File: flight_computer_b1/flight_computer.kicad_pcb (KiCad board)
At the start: 4 copper layers, 78 x 67 mm, 102 parts, among them J1 DB25_Socket, J2 DB25_Socket, J3 Conn_01x03, J4 Screw_Terminal_01x02, J5 Pi Connector, J6 Conn_02x02_Odd_Even, Q3 ISA170230C04LMDS, U1 IRLML6344TRPBF, U10 LTC2983, U11 CD74HC4067SM, U12 IRLML6344TRPBF, U2 IRLML6344TRPBF, U3 IRLML6344TRPBF, U4 IRLML6344TRPBF, U5 LMR51430XFDDCR, U6 MCP6001-OT, U7 MCP6001-OT, U8 ADS1158IRTCR, U9 LM66200DRLR, Y1 32.768kHz

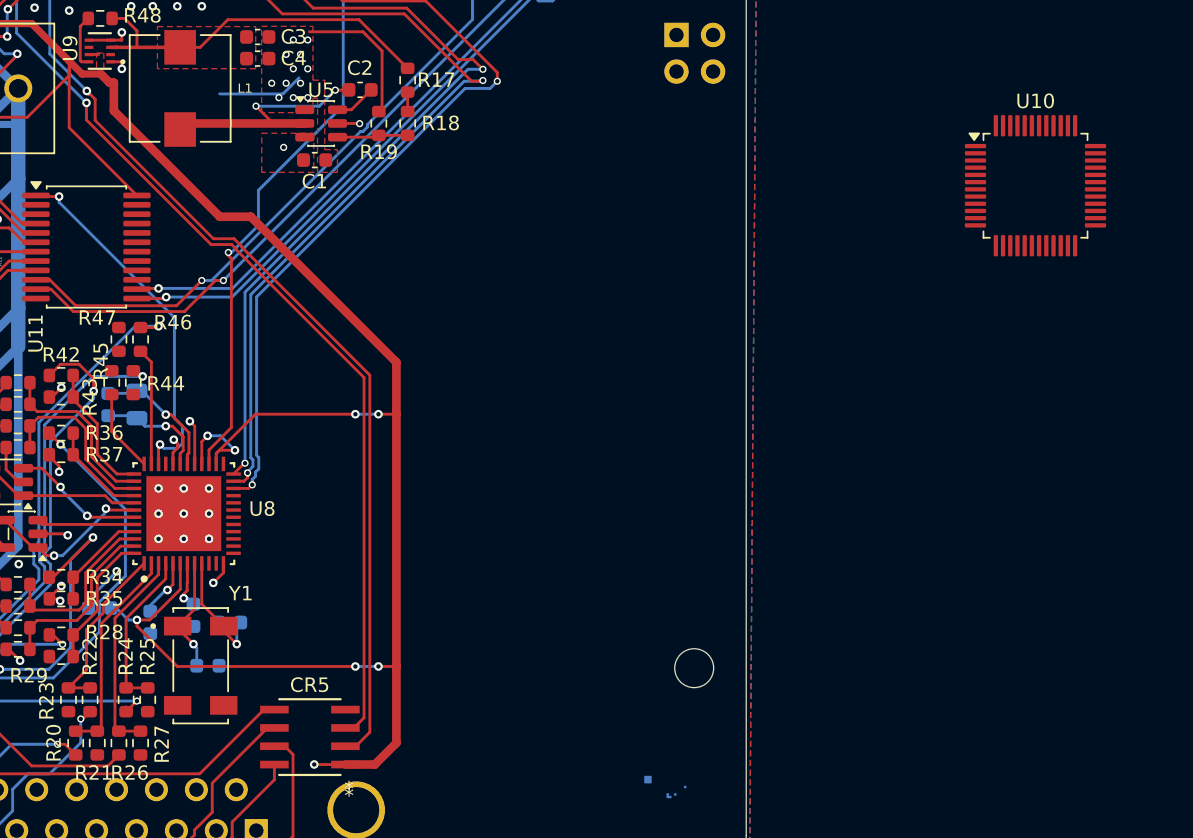
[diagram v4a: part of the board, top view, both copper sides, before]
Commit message: assigned footprints to capacitors
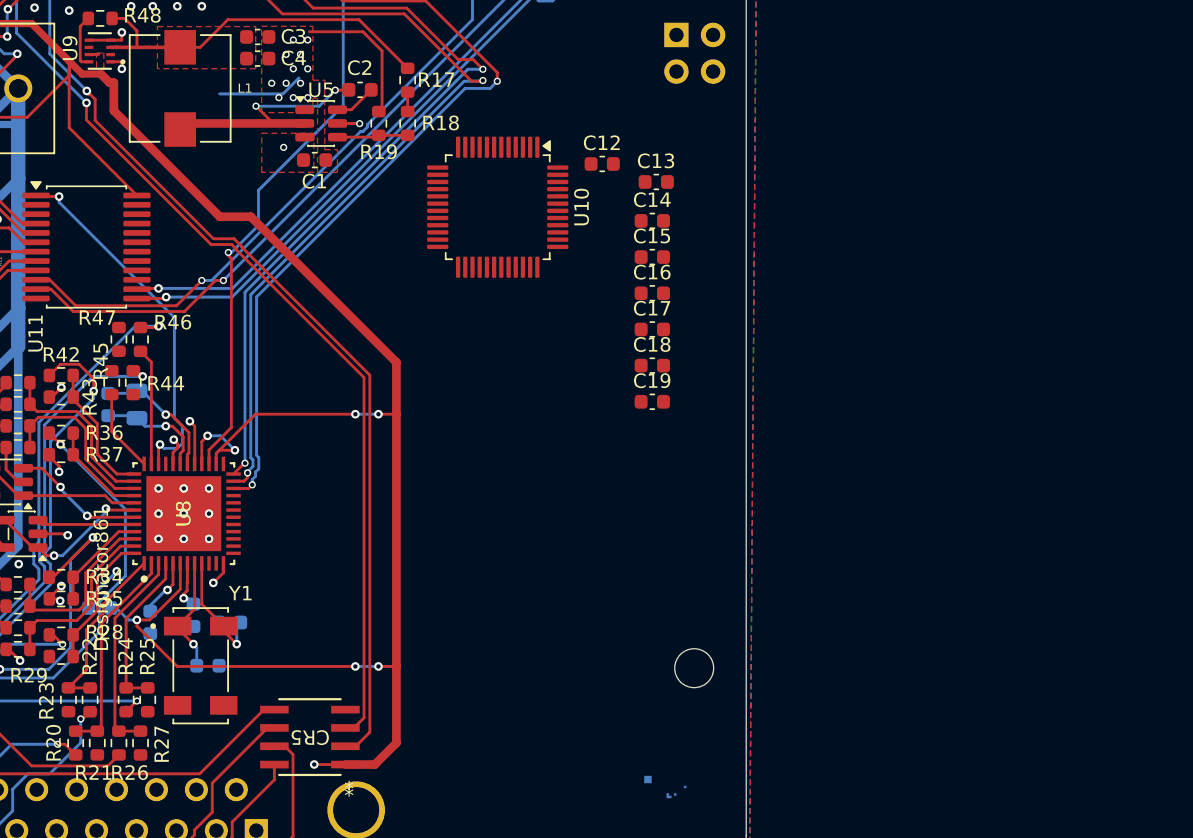
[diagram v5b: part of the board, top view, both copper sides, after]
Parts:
- added C12: 10uF, Capacitor_SMD:C_0603_1608Metric, F.Cu at (170.5, 88.8)
- added C13: 10uF, Capacitor_SMD:C_0603_1608Metric, F.Cu at (174.2, 90.0)
- added C14: 10uF, Capacitor_SMD:C_0603_1608Metric, F.Cu at (174.0, 92.7)
- added C15: 10uF, Capacitor_SMD:C_0603_1608Metric, F.Cu at (174.0, 95.2)
- added C16: 0.1uF, Capacitor_SMD:C_0603_1608Metric, F.Cu at (174.0, 97.7)
- added C17: 0.1uF, Capacitor_SMD:C_0603_1608Metric, F.Cu at (174.0, 100.2)
- added C18: 0.1uF, Capacitor_SMD:C_0603_1608Metric, F.Cu at (174.0, 102.7)
- added C19: 0.1uF, Capacitor_SMD:C_0603_1608Metric, F.Cu at (174.0, 105.2)
- CR5: footprint avi_lib:SO-8_STM -> avi_footprint:SO-8_STM
- U8: footprint avi_lib:RTC0048A-IPC_A -> avi_footprint:RTC0048A-IPC_A
- moved U10 37.3 mm to (163.2, 91.8), turned to -90 degrees

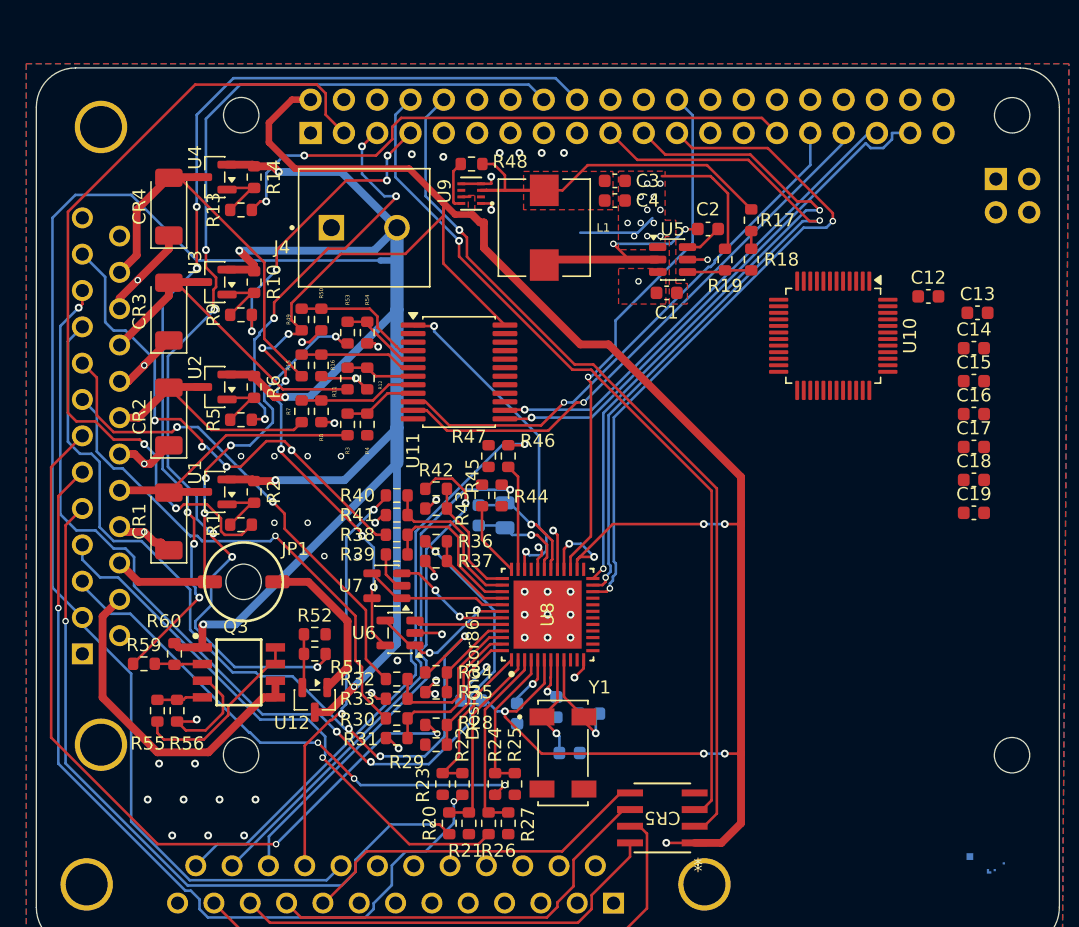
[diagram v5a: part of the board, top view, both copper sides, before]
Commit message: routed traces for pi & fixed many DRC issues
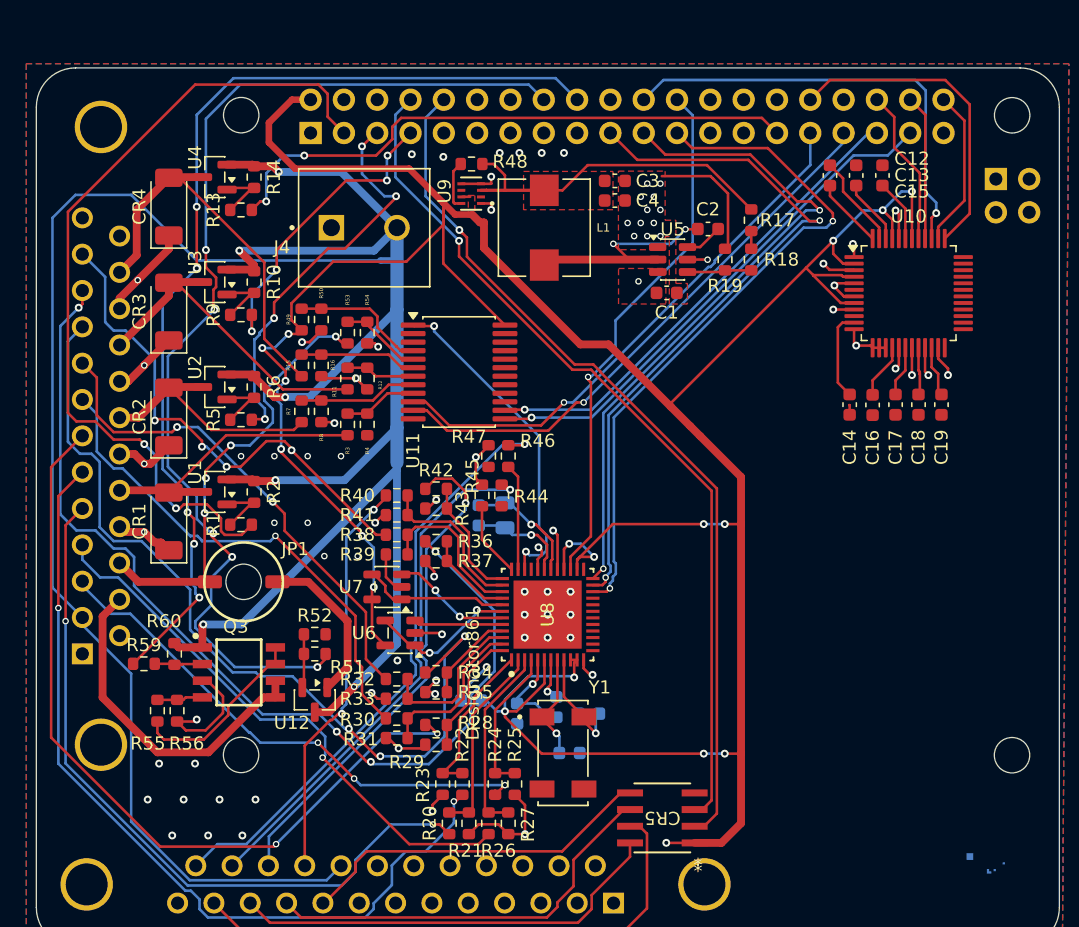
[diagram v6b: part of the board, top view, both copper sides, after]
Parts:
- moved C15 17.2 mm to (167.0, 79.5), turned to 90 degrees
- moved C13 14.0 mm to (165.0, 79.5), turned to 90 degrees
- moved C12 11.9 mm to (163.0, 79.5), turned to 90 degrees
- moved C14 10.4 mm to (164.5, 97.0), turned to -90 degrees
- moved C19 8.61 mm to (171.5, 97.0), turned to -90 degrees
- moved C16 7.76 mm to (166.2, 97.0), turned to -90 degrees
- moved C18 7.13 mm to (169.8, 97.0), turned to -90 degrees
- moved C17 6.79 mm to (168.0, 97.0), turned to -90 degrees
- moved U10 6.60 mm to (169.0, 88.5), turned to 0 degrees
- moved U7 0.09 mm to (129.2, 110.9)
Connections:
- J5 pad 22: unconnected-(J5-Pin_22-Pad22) -> /TEMP_DOUT
- J5 pad 32: unconnected-(J5-Pin_32-Pad32) -> /TEMP_INT
- J5 pad 35: /TEMP_DOUT -> /mux_addr2
- J5 pad 37: unconnected-(J5-Pin_37-Pad37) -> /mux_addr3
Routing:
- net +5V: track 193.3 -> 244.8 mm, vias 14 -> 18
- net GND: track 182.2 -> 219.4 mm, vias 70 -> 83
- net /TEMP_DOUT: track 0.00 -> 34.2 mm, vias 0 -> 1
- net /TEMP_INT: track 0.00 -> 24.6 mm
- net /TEMP_SCLK: track 0.00 -> 12.1 mm
- net /TEMP_CS: track 0.00 -> 12.0 mm
- net /TEMP_DIN: track 0.00 -> 11.1 mm
- net Net-(U10-Q2): track 0.00 -> 7.14 mm
- net Net-(U10-V_{REF_BYP}): track 0.00 -> 6.88 mm
- net Net-(U10-Q1): track 0.00 -> 5.38 mm
- net Net-(U10-Q3): track 0.00 -> 4.97 mm
- net Net-(U10-LDO): track 0.00 -> 4.76 mm
- net /TC1+: track 0.00 -> 4.21 mm
- net /TC4+: track 0.00 -> 3.87 mm
- net /TC2+: track 0.00 -> 3.87 mm
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
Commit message: net updates
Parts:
- removed G***: LOGO, avi_lib:qr-code
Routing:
- net GND: vias 83 -> 85

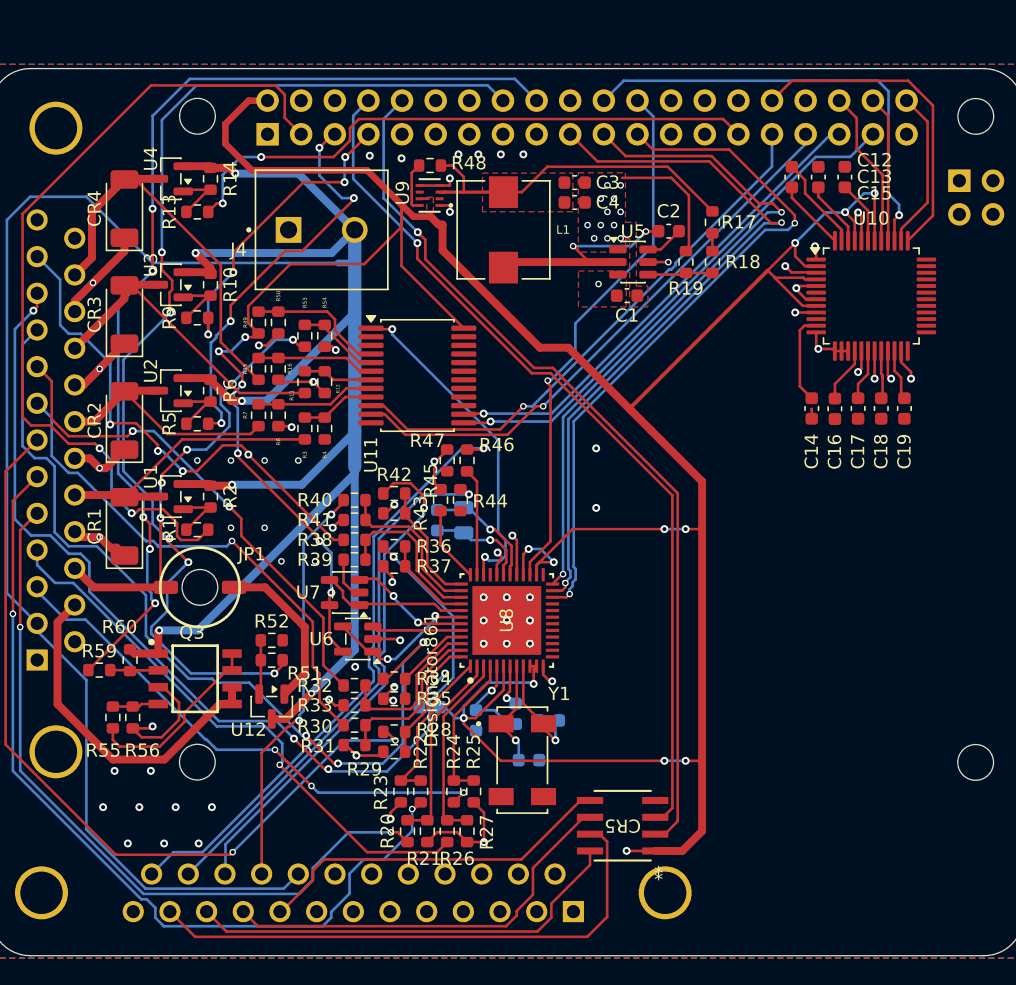
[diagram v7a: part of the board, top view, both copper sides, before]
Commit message: routed pi traces, fixed all unavoidable DRC errors
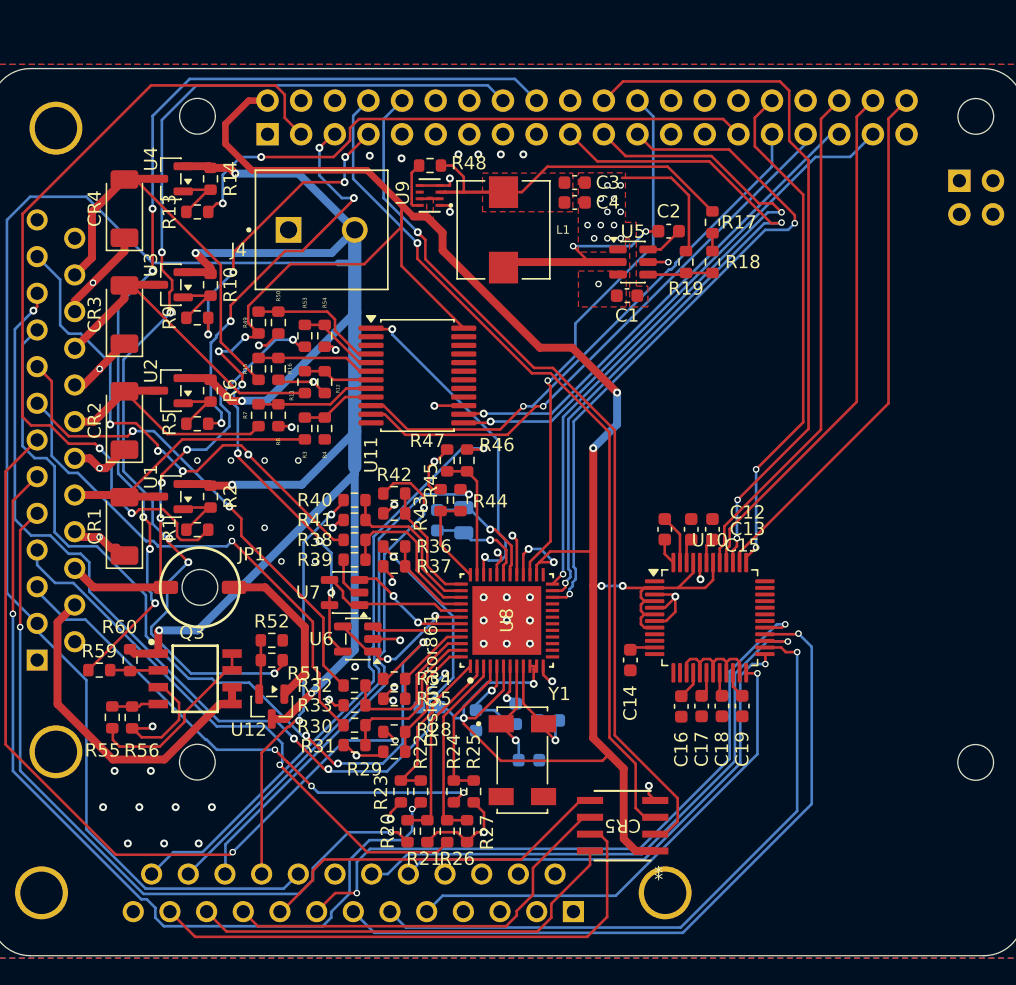
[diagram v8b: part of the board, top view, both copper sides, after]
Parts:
- moved C15 28.4 mm to (157.0, 106.1)
- moved C12 28.3 mm to (153.4, 106.1)
- moved C13 28.3 mm to (155.4, 106.1)
- moved U10 27.2 mm to (156.8, 112.8)
- moved C19 25.6 mm to (159.2, 119.5)
- moved C18 25.5 mm to (157.7, 119.5)
- moved C17 25.4 mm to (156.2, 119.5)
- moved C16 25.3 mm to (154.7, 119.5)
- moved C14 23.4 mm to (150.8, 116.0)
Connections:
- J1 pad 18: unconnected-(J1-P18-Pad18) -> /OX_RTD_UPPER_B
- J1 pad 19: unconnected-(J1-P19-Pad19) -> /OX_RTD_LOWER_A
- J1 pad 5: unconnected-(J1-Pad5) -> /OX_RTD_UPPER_A
- J1 pad 6: unconnected-(J1-Pad6) -> /OX_RTD_UPPER_C
- J1 pad 7: unconnected-(J1-Pad7) -> /OX_RTD_LOWER_B
- J1 pad 8: unconnected-(J1-Pad8) -> /OX_RTD_LOWER_C
- J4 pad 2: GND -> GND24V
- NT1 pad 2: GND -> GND24V
- Q3 pad 1: GND -> GND24V
- R10 pad 2: GND -> GND24V
- R14 pad 2: GND -> GND24V
- R2 pad 2: GND -> GND24V
- R6 pad 2: GND -> GND24V
- R60 pad 2: GND -> GND24V
- U1 pad 2: GND -> GND24V
- U10 pad 24: /RTD1A -> /OX_RTD_UPPER_A
- U10 pad 25: /RTD1B -> /OX_RTD_UPPER_B
- U10 pad 26: /RTD1C -> /OX_RTD_UPPER_C
- U10 pad 27: /RTD2A -> /OX_RTD_LOWER_A
- U10 pad 28: /RTD2B -> /OX_RTD_LOWER_B
- U10 pad 29: /RTD2C -> /OX_RTD_LOWER_C
- U12 pad 3: GND -> GND24V
- U2 pad 2: GND -> GND24V
- U3 pad 2: GND -> GND24V
- U4 pad 2: GND -> GND24V
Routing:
- net GND: track 219.4 -> 90.3 mm, vias 85 -> 71
- net GND24V: track 0.00 -> 127.4 mm, vias 0 -> 6
- net /OX_RTD_LOWER_B: track 0.00 -> 55.2 mm, vias 0 -> 1
- net /OX_RTD_LOWER_C: track 0.00 -> 51.3 mm, vias 0 -> 2
- net /OX_RTD_UPPER_C: track 0.00 -> 49.5 mm, vias 0 -> 1
- net /OX_RTD_LOWER_A: track 0.00 -> 44.3 mm, vias 0 -> 1
- net +5V: track 244.8 -> 203.1 mm, vias 18 -> 14
- net /OX_RTD_UPPER_B: track 0.00 -> 38.2 mm, vias 0 -> 1
- net /OX_RTD_UPPER_A: track 0.00 -> 36.9 mm, vias 0 -> 1
- net /TEMP_DIN: track 11.1 -> 39.5 mm
- net /TEMP_SCLK: track 12.1 -> 40.1 mm
- net /TEMP_CS: track 12.0 -> 38.6 mm
- net /TEMP_DOUT: track 34.2 -> 53.5 mm, vias 1 -> 2
- net /TEMP_INT: track 24.6 -> 38.7 mm, vias 0 -> 2
- net Net-(U10-V_{REF_BYP}): track 6.88 -> 1.91 mm
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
